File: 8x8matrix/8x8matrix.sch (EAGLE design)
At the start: 3 parts

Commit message: alt
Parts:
- added JP1: (no value), SparkFun-Connectors:M05PTH
- added JP2: (no value), SparkFun-Connectors:M081X08
- added R1, R2: 1k, microbuilder:RESISTOR0805_NOTHERMALS
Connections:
- removed net N$27: U$2.LATCH, U$3.LATCH
- new net CLK: JP1.4, U$2.CLK, U$3.CLK
- new net LATCH: JP1.5, U$2.LATCH, U$3.LATCH
- new net N$28: R1.2, U$3.RSET
- new net N$29: R2.2, U$2.RSET
- new net N$30: JP2.2, U$1.R3
- new net N$31: JP2.3, U$1.R2
- new net N$32: JP2.4, U$1.R1
- new net N$33: JP2.6, U$1.R6
- new net N$34: JP2.7, U$1.R7
- new net N$35: JP2.8, U$1.R8
- new net SIN: JP1.3, U$3.SIN
- new net SOUT: U$2.SIN, U$3.SOUT
- net 5.0V: now also JP1.2
- net GND: now also JP1.1, R1.1, R2.1
- net N$1: now also U$1.C8B; no longer U$1.C1R
- net N$10: now also U$1.C2G, U$3.LED2; no longer U$1.C4R, U$2.LED10
- net N$11: now also U$1.C3G, U$3.LED3; no longer U$1.C4G, U$2.LED11
- net N$12: now also U$1.C4G, U$3.LED4; no longer U$1.C4B, U$2.LED12
- net N$13: now also U$1.C5G, U$3.LED5; no longer U$1.C5R, U$2.LED13
- net N$14: now also U$1.C6G, U$3.LED6; no longer U$1.C5G, U$2.LED14
- net N$15: now also U$1.C7G, U$3.LED7; no longer U$1.C5B, U$2.LED15
- net N$16: now also U$1.C8G, U$3.LED8; no longer U$1.C6R, U$2.LED16
- net N$17: now also U$1.C8R, U$3.LED9; no longer U$1.C6G, U$3.LED1
- net N$18: now also U$1.C7R, U$3.LED10; no longer U$1.C6B, U$3.LED2
- net N$19: now also U$1.C6R, U$3.LED11; no longer U$1.C7R, U$3.LED3
- net N$2: now also U$1.C7B; no longer U$1.C1G
- net N$20: now also U$1.C5R, U$3.LED12; no longer U$1.C7G, U$3.LED4
- net N$21: now also U$1.C4R, U$3.LED13; no longer U$1.C7B, U$3.LED5
- net N$22: now also U$1.C3R, U$3.LED14; no longer U$1.C8R, U$3.LED6
- net N$23: now also U$1.C2R, U$3.LED15; no longer U$1.C8G, U$3.LED7
- net N$24: now also U$1.C1R, U$3.LED16; no longer U$1.C8B, U$3.LED8
- net N$25: now also JP2.5, U$1.R5; no longer U$2.CLK, U$3.CLK
- net N$26: now also JP2.1, U$1.R4; no longer U$2.SOUT, U$3.SIN
- net N$3: now also U$1.C6B; no longer U$1.C1B
- net N$4: now also U$1.C5B; no longer U$1.C2R
- net N$5: now also U$1.C4B; no longer U$1.C2G
- net N$6: now also U$1.C3B; no longer U$1.C2B
- net N$7: now also U$1.C2B; no longer U$1.C3R
- net N$8: now also U$1.C1B; no longer U$1.C3G
- net N$9: now also U$1.C1G, U$3.LED1; no longer U$1.C3B, U$2.LED9

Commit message: tlc
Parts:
- removed JP2: (no value), SparkFun-Connectors:M081X08
- removed R2: 1k, microbuilder:RESISTOR0805_NOTHERMALS
- removed U$2, U$3: CAT4016W, CAT4016:CAT4016W
- added IC1: 74595, SparkFun-DigitalIC:74595
- added U$14: TLC5947DAP, TLC5947:TLC5947DAP
- JP1: device SparkFun-Connectors:M05PTH -> SparkFun-Connectors:M06SIP
- R1: value 1k -> (none); device microbuilder:RESISTOR0805_NOTHERMALS -> resistor:R-US_R0805
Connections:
- removed net CLK: JP1.4, U$2.CLK, U$3.CLK
- removed net LATCH: JP1.5, U$2.LATCH, U$3.LATCH
- removed net N$35: JP2.8, U$1.R8
- removed net SOUT: U$2.SIN, U$3.SOUT
- new net BLANK: JP1.3, U$14.BLANK
- new net N$27: R1.2, U$14.IREF
- new net XLAT: JP1.6, U$14.XLAT
- net 5.0V: now also JP1.4, U$14.VCC; no longer JP1.2, U$2.VDD, U$3.VDD
- net GND: now also JP1.5, U$14.GND, U$14.PAD; no longer JP1.1, R2.1, U$2.BLANK, U$2.GND, U$3.BLANK, U$3.GND
- net N$1: now also U$1.C1B, U$14.OUT0; no longer U$1.C8B, U$2.LED1
- net N$10: now also U$1.C2R, U$14.OUT9; no longer U$1.C2G, U$3.LED2
- net N$11: now also U$1.C3R, U$14.OUT10; no longer U$1.C3G, U$3.LED3
- net N$12: now also U$1.C4R, U$14.OUT11; no longer U$1.C4G, U$3.LED4
- net N$13: now also U$1.C5R, U$14.OUT12; no longer U$1.C5G, U$3.LED5
- net N$14: now also U$1.C6R, U$14.OUT13; no longer U$1.C6G, U$3.LED6
- net N$15: now also U$1.C7R, U$14.OUT14; no longer U$1.C7G, U$3.LED7
- net N$16: now also U$1.C8R, U$14.OUT15; no longer U$1.C8G, U$3.LED8
- net N$17: now also U$1.C8G, U$14.OUT16; no longer U$1.C8R, U$3.LED9
- net N$18: now also U$1.C7G, U$14.OUT17; no longer U$1.C7R, U$3.LED10
- net N$19: now also U$1.C6G, U$14.OUT18; no longer U$1.C6R, U$3.LED11
- net N$2: now also U$1.C2B, U$14.OUT1; no longer U$1.C7B, U$2.LED2
- net N$20: now also U$1.C5G, U$14.OUT19; no longer U$1.C5R, U$3.LED12
- net N$21: now also U$1.C4G, U$14.OUT20; no longer U$1.C4R, U$3.LED13
- net N$22: now also U$1.C3G, U$14.OUT21; no longer U$1.C3R, U$3.LED14
- net N$23: now also U$1.C2G, U$14.OUT22; no longer U$1.C2R, U$3.LED15
- net N$24: now also U$1.C1G, U$14.OUT23; no longer U$1.C1R, U$3.LED16
- net N$25: now also IC1.QB; no longer JP2.5
- net N$26: now also IC1.QC, U$1.R6; no longer JP2.1, U$1.R4
- net N$28: now also JP1.2, U$14.SCLK; no longer R1.2, U$3.RSET
- net N$29: now also IC1.QD, U$1.R7; no longer R2.2, U$2.RSET
- net N$3: now also U$1.C3B, U$14.OUT2; no longer U$1.C6B, U$2.LED3
- net N$30: now also IC1.QE, U$1.R8; no longer JP2.2, U$1.R3
- net N$31: now also IC1.QF, U$1.R4; no longer JP2.3, U$1.R2
- net N$32: now also IC1.QG, U$1.R3; no longer JP2.4, U$1.R1
- net N$33: now also IC1.QH, U$1.R2; no longer JP2.6, U$1.R6
- net N$34: now also IC1.QH*, U$1.R1; no longer JP2.7, U$1.R7
- net N$4: now also U$1.C4B, U$14.OUT3; no longer U$1.C5B, U$2.LED4
- net N$5: now also U$1.C5B, U$14.OUT4; no longer U$1.C4B, U$2.LED5
- net N$6: now also U$1.C6B, U$14.OUT5; no longer U$1.C3B, U$2.LED6
- net N$7: now also U$1.C7B, U$14.OUT6; no longer U$1.C2B, U$2.LED7
- net N$8: now also U$1.C8B, U$14.OUT7; no longer U$1.C1B, U$2.LED8
- net N$9: now also U$1.C1R, U$14.OUT8; no longer U$1.C1G, U$3.LED1
- net SIN: now also JP1.1, U$14.SIN; no longer JP1.3, U$3.SIN

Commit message: tlc2
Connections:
- net 5.0V: now also IC1.VCC
- net GND: now also IC1.GND
- net N$34: now also IC1.QA; no longer IC1.QH*
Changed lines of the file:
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@@
 <part name="IC1" library="SparkFun-DigitalIC" deviceset="74*595" device=""/>
 <part name="U$3" library="microbuilder" deviceset="GND" device=""/>
+<part name="U$4" library="microbuilder" deviceset="GND" device=""/>
+<part name="U$5" library="microbuilder" deviceset="5.0V" device=""/>
 </parts>
 <sheets>
@@
 <instance part="IC1" gate="A" x="-10.16" y="60.96"/>
 <instance part="U$3" gate="G$1" x="-10.16" y="160.02" rot="R270"/>
+<instance part="U$4" gate="G$1" x="-20.32" y="45.72"/>
+<instance part="U$5" gate="G$1" x="5.08" y="73.66"/>
 </instances>
 <busses>
@@
 <pinref part="U$3" gate="G$1" pin="GND"/>
 </segment>
+<segment>
+<pinref part="IC1" gate="A" pin="GND"/>
+<pinref part="U$4" gate="G$1" pin="GND"/>
+</segment>
 </net>
 <net name="5.0V" class="0">
@@
 <pinref part="JP1" gate="G$1" pin="4"/>
 <pinref part="U$12" gate="G$1" pin="5.0V"/>
+</segment>
+<segment>
+<pinref part="IC1" gate="A" pin="VCC"/>
+<pinref part="U$5" gate="G$1" pin="5.0V"/>
 </segment>
 </net>
@@
 <net name="N$34" class="0">
 <segment>
-<pinref part="IC1" gate="A" pin="QH*"/>
-<wire x1="5.08" y1="48.26" x2="10.16" y2="48.26" width="0.1524" layer="91"/>
-<wire x1="10.16" y1="48.26" x2="10.16" y2="109.22" width="0.1524" layer="91"/>
+<pinref part="IC1" gate="A" pin="QA"/>
+<wire x1="5.08" y1="68.58" x2="10.16" y2="68.58" width="0.1524" layer="91"/>
+<wire x1="10.16" y1="68.58" x2="10.16" y2="109.22" width="0.1524" layer="91"/>
 <pinref part="U$1" gate="G$1" pin="R1"/>
 <wire x1="10.16" y1="109.22" x2="30.48" y2="109.22" width="0.1524" layer="91"/>

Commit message: tlc3
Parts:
- removed IC1: 74595, SparkFun-DigitalIC:74595
- removed JP1: (no value), SparkFun-Connectors:M06SIP
- added JP2: M09, SparkFun-Connectors:M09
- added R2: 0R, resistor:R-US_M1206
- added U$9: CD74HC238M, mylib:CD74HC238M
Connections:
- removed net XLAT: JP1.6, U$14.XLAT
- new net N$35: U$1.R5, U$9.Y7
- net 5.0V: now also JP2.6, U$9.E3, U$9.VCC; no longer IC1.VCC, JP1.4
- net BLANK: now also JP2.3; no longer JP1.3
- net GND: now also JP2.5, R2.1, R2.2, U$9.E1, U$9.E2, U$9.GND; no longer IC1.GND, JP1.5
- net N$25: now also JP2.4, U$14.XLAT; no longer IC1.QB, U$1.R5
- net N$26: now also U$9.Y6; no longer IC1.QC
- net N$28: now also JP2.2; no longer JP1.2
- net N$29: now also U$9.Y5; no longer IC1.QD
- net N$30: now also U$9.Y4; no longer IC1.QE
- net N$31: now also U$9.Y3; no longer IC1.QF
- net N$32: now also U$9.Y2; no longer IC1.QG
- net N$33: now also U$9.Y1; no longer IC1.QH
- net N$34: now also U$9.Y0; no longer IC1.QA
- net SIN: now also JP2.1; no longer JP1.1

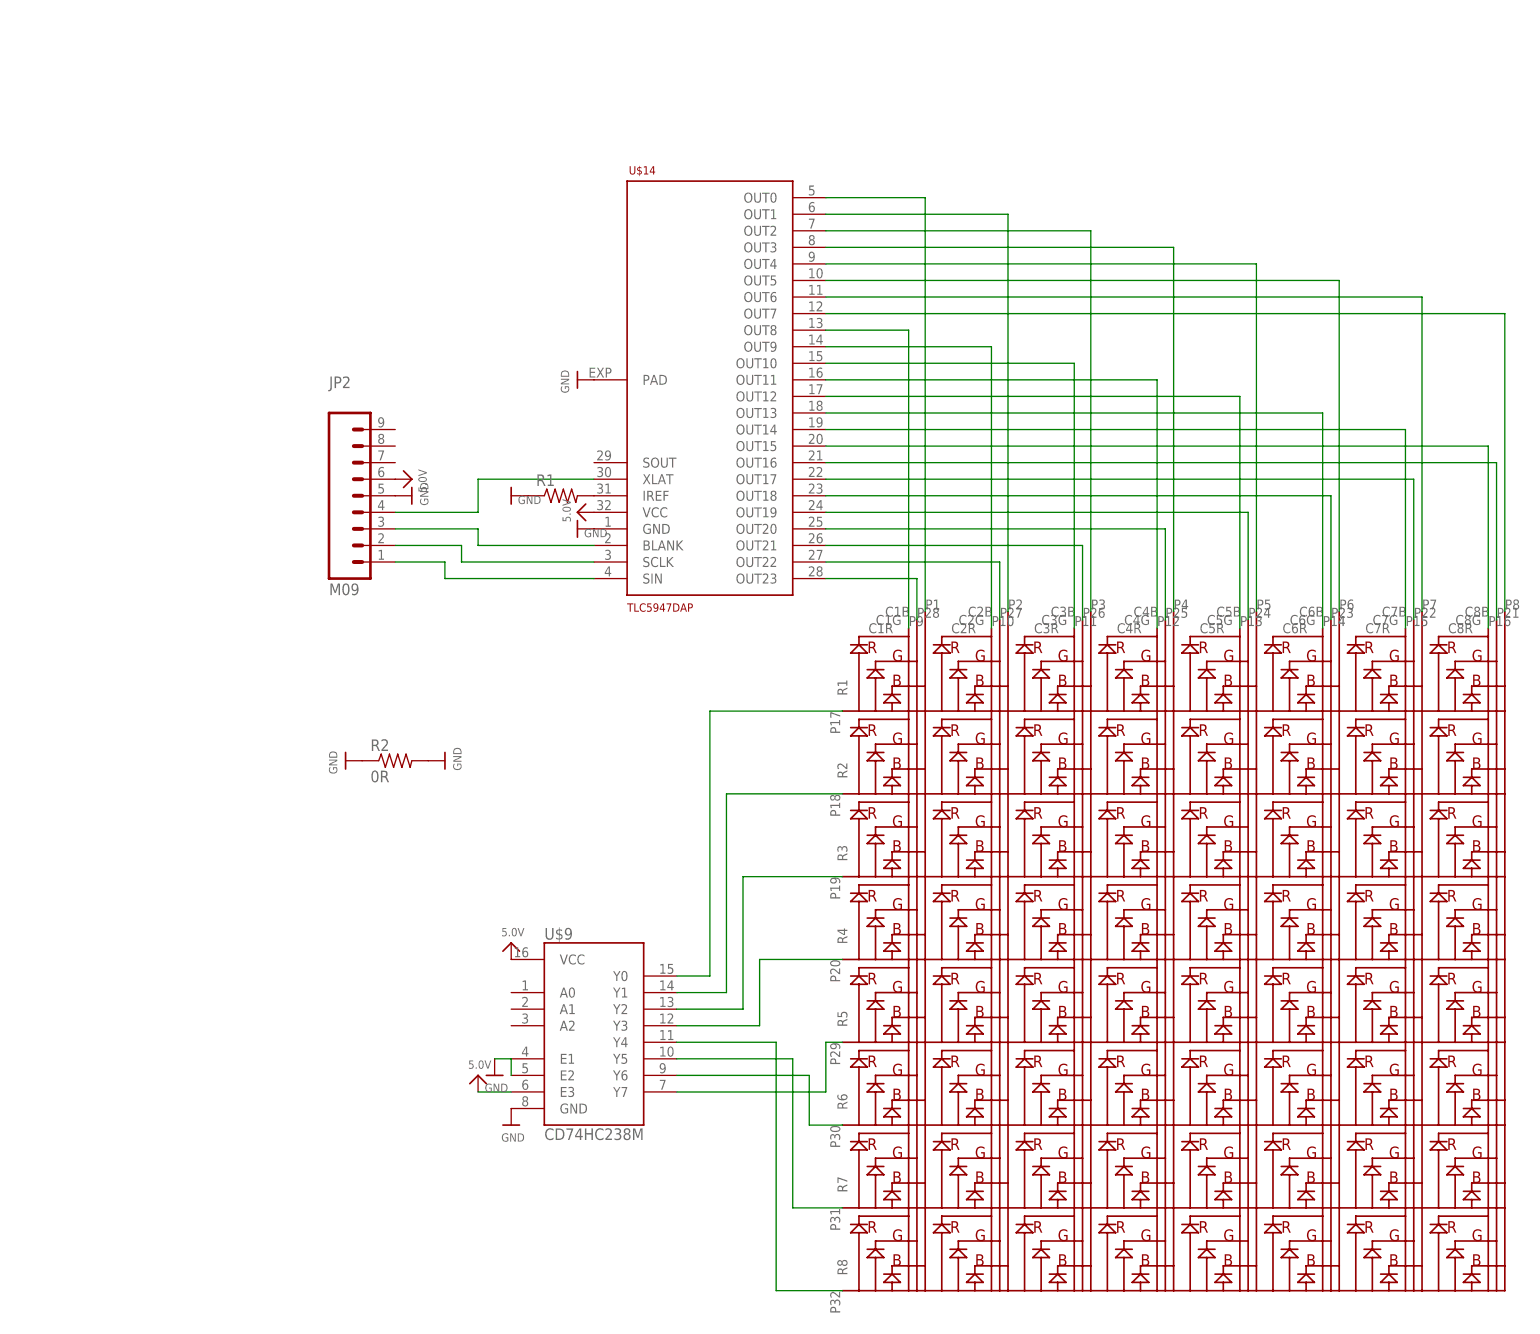
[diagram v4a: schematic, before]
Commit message: tried adding FZTA92 darlingtons
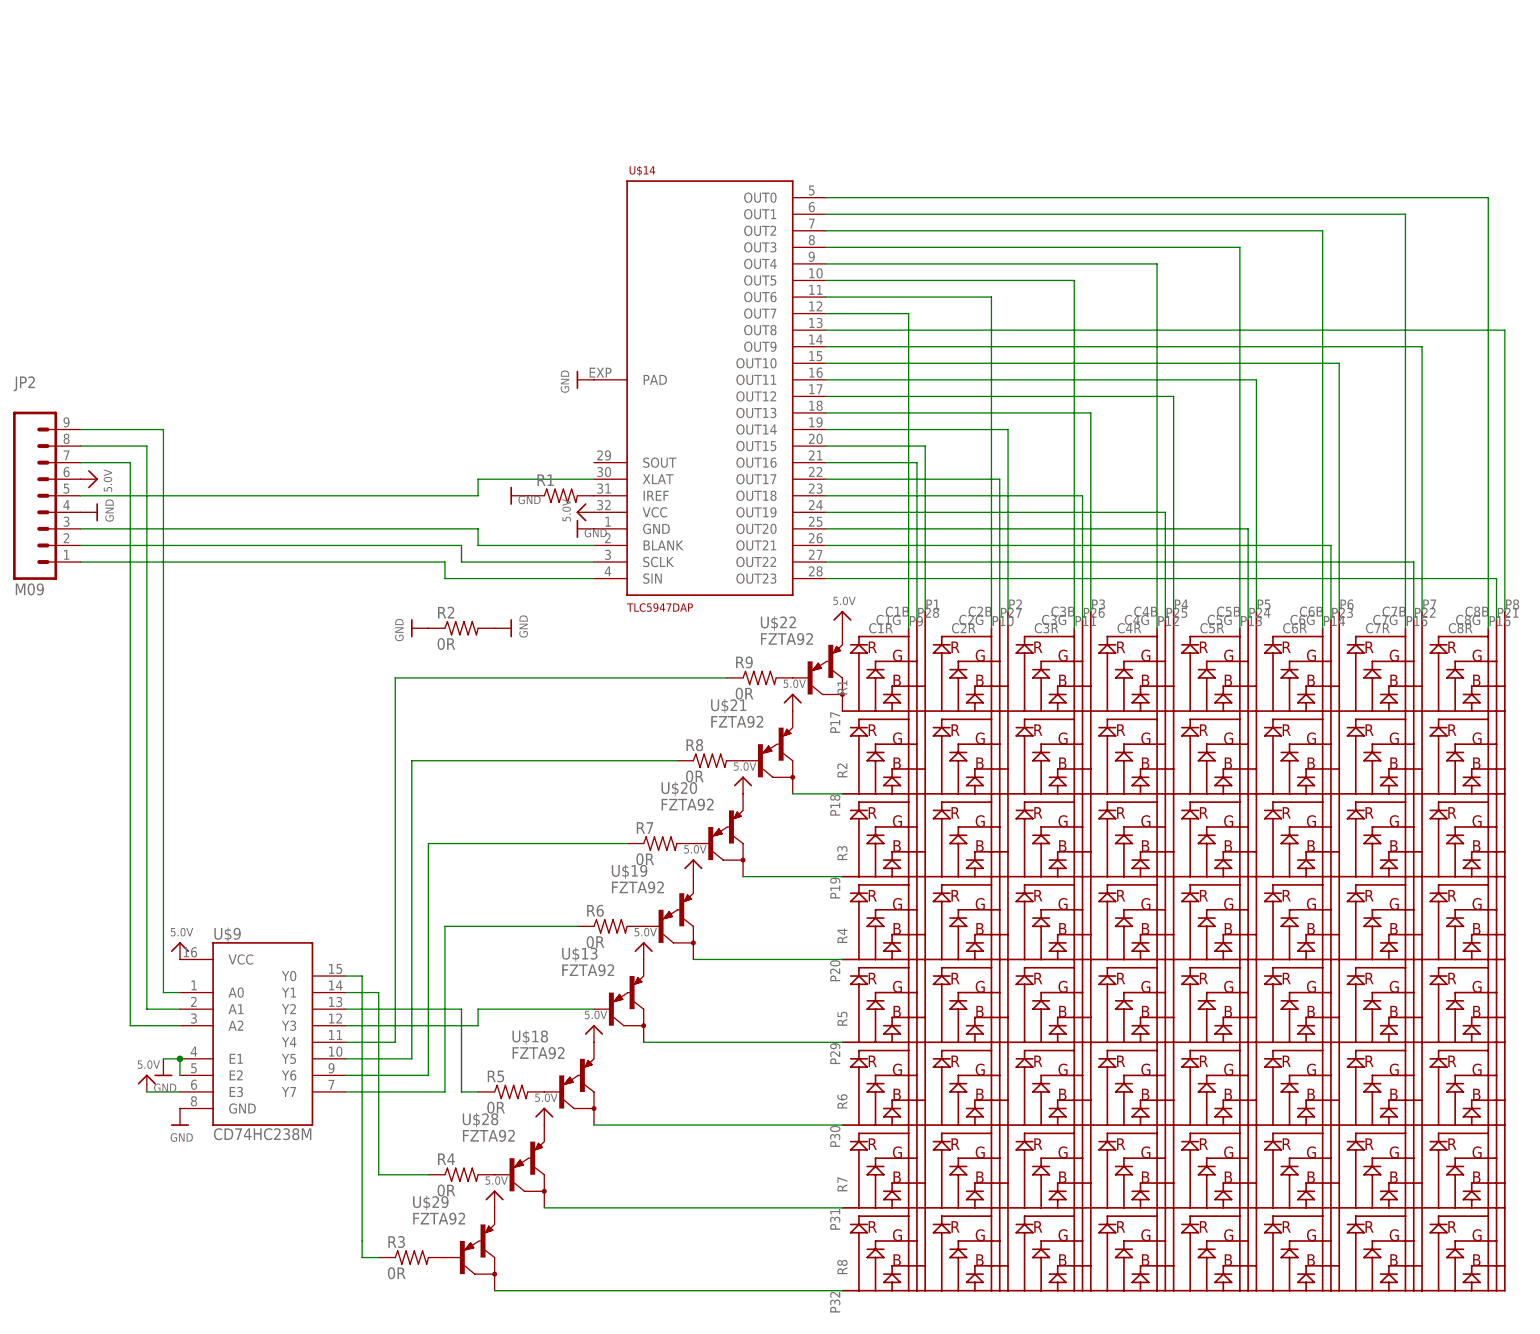
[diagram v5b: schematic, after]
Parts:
- added R3, R4, R5, R6, R7, R8, R9: 0R, resistor:R-US_M1206
- added U$13, U$18, U$19, U$20, U$21, U$22, U$28, U$29: FZTA92, mylib:FZTA92
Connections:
- net N$28 renamed SCLK
- new net N$28: R5.2, U$18.B
- new net N$36: JP2.9, U$9.A0
- new net N$37: JP2.8, U$9.A1
- new net N$38: JP2.7, U$9.A2
- new net N$39: R7.2, U$20.B
- new net N$40: R8.2, U$21.B
- new net N$41: R9.2, U$22.B
- new net N$42: U$1.R6, U$18.C
- new net N$43: U$1.R1, U$22.C
- new net N$44: U$1.R2, U$21.C
- new net N$45: R6.2, U$19.B
- new net N$46: U$1.R3, U$20.C
- new net N$47: U$1.R4, U$19.C
- new net N$48: R4.2, U$28.B
- new net N$49: R3.2, U$29.B
- new net N$50: U$1.R7, U$28.C
- new net N$51: U$1.R8, U$29.C
- new net XLAT: JP2.5, U$14.XLAT
- net 5.0V: now also U$13.E, U$18.E, U$19.E, U$20.E, U$21.E, U$22.E, U$28.E, U$29.E
- net GND: now also JP2.4; no longer JP2.5
- net N$1: now also U$1.C8R; no longer U$1.C1B
- net N$10: now also U$1.C7B; no longer U$1.C2R
- net N$11: now also U$1.C6B; no longer U$1.C3R
- net N$12: now also U$1.C5B; no longer U$1.C4R
- net N$13: now also U$1.C4B; no longer U$1.C5R
- net N$14: now also U$1.C3B; no longer U$1.C6R
- net N$15: now also U$1.C2B; no longer U$1.C7R
- net N$16: now also U$1.C1B; no longer U$1.C8R
- net N$17: now also U$1.C1G; no longer U$1.C8G
- net N$18: now also U$1.C2G; no longer U$1.C7G
- net N$19: now also U$1.C3G; no longer U$1.C6G
- net N$2: now also U$1.C7R; no longer U$1.C2B
- net N$20: now also U$1.C4G; no longer U$1.C5G
- net N$21: now also U$1.C5G; no longer U$1.C4G
- net N$22: now also U$1.C6G; no longer U$1.C3G
- net N$23: now also U$1.C7G; no longer U$1.C2G
- net N$24: now also U$1.C8G; no longer U$1.C1G
- net N$25: now also U$13.B, U$9.Y3; no longer JP2.4, U$14.XLAT
- net N$26: now also R6.1, U$9.Y7; no longer U$1.R6, U$9.Y6
- net N$29: now also R7.1, U$9.Y6; no longer U$1.R7, U$9.Y5
- net N$3: now also U$1.C6R; no longer U$1.C3B
- net N$30: now also R8.1, U$9.Y5; no longer U$1.R8, U$9.Y4
- net N$31: now also R9.1, U$9.Y4; no longer U$1.R4, U$9.Y3
- net N$32: now also U$1.R5, U$13.C; no longer U$1.R3, U$9.Y2
- net N$33: now also R5.1, U$9.Y2; no longer U$1.R2, U$9.Y1
- net N$34: now also R4.1, U$9.Y1; no longer U$1.R1, U$9.Y0
- net N$35: now also R3.1, U$9.Y0; no longer U$1.R5, U$9.Y7
- net N$4: now also U$1.C5R; no longer U$1.C4B
- net N$5: now also U$1.C4R; no longer U$1.C5B
- net N$6: now also U$1.C3R; no longer U$1.C6B
- net N$7: now also U$1.C2R; no longer U$1.C7B
- net N$8: now also U$1.C1R; no longer U$1.C8B
- net N$9: now also U$1.C8B; no longer U$1.C1R
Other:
- moved on the sheet: JP2, R2, U$9
